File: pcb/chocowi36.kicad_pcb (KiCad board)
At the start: 2 copper layers, 113.1 x 88.3 mm, 29 parts, among them SW10 SW_Push, SW11 SW_Push, SW12 SW_Push, SW14 SW_Push, SW15 SW_Push, SW16 SW_Push, SW17 SW_Push, SW18 SW_Push, SW19 SW_Push, SW2 SW_Push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

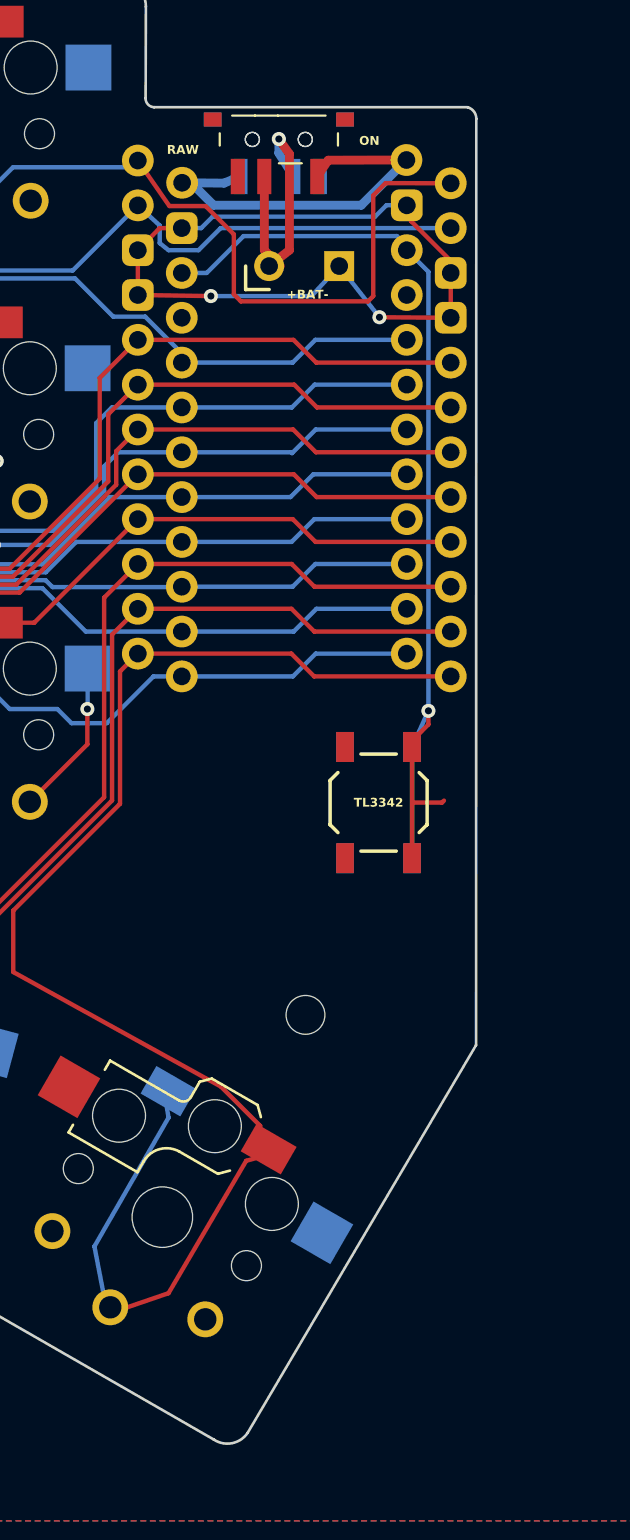
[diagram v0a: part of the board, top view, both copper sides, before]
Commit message: add tp4056 charging module, update edge.cut
change power button position
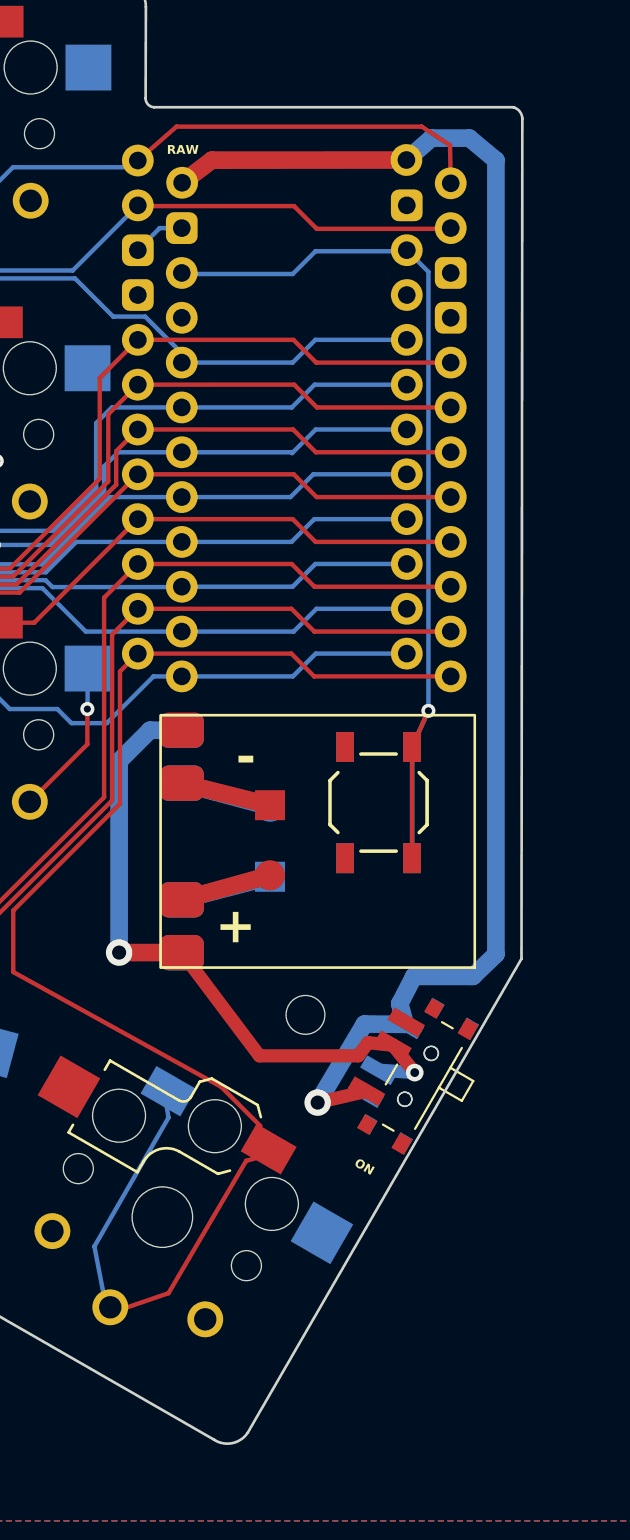
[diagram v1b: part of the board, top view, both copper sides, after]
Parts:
- added BT2: B1, itsdmd:Battery_Pads-dual-side, B.Cu at (176.6, 101.4)
- added T1: ~, itsdmd:Module_TP4056_Mini-SMD_Interface, F.Cu at (179.2, 101.5)
- added T2: ~, itsdmd:Module_TP4056_Mini-SMD_Interface, B.Cu at (179.2, 101.5)
- BT1: value Battery_Cell -> B1
- moved SW_POWER1 53.8 mm to (184.8, 115.0), turned to 60 degrees
- moved SW_POWER2 53.6 mm to (185.0, 114.7), turned to -120 degrees
- moved BT1 32.7 mm to (176.6, 101.5), turned to 90 degrees
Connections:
- BT1 pad 2: gnd -> Net-(BT1--)
- SW_POWER1 pad COM: Net-(BT1-+) -> Net-(T1-Load+)
- SW_POWER2 pad COM: Net-(BT1-+) -> Net-(T1-Load+)
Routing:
- net +BATT: track 23.2 -> 82.6 mm, vias 0 -> 1
- net gnd: track 55.8 -> 12.9 mm, vias 3 -> 1
- net Net-(T1-Load+): track 0.00 -> 38.2 mm, vias 0 -> 2
- net Net-(BT1-+): track 15.7 -> 5.19 mm, vias 1 -> 0
- net Switch6: track 69.5 -> 61.0 mm
- net Net-(BT2-+): track 0.00 -> 5.18 mm
- net Net-(BT2--): track 0.00 -> 5.17 mm
- net Net-(BT1--): track 0.00 -> 5.15 mm
- net reset: track 59.8 -> 57.0 mm
- net Switch5: track 79.4 -> 77.9 mm
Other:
- board size 113.1 x 88.3 mm -> 115.7 x 88.3 mm
- board text removed: "+BAT-"
- board text removed: "-BAT+"

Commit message: minor improvements
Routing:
- net gnd: track 12.9 -> 9.84 mm
- net reset: track 57.0 -> 57.7 mm

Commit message: slight changes
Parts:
- moved BT1 11.6 mm to (166.4, 107.1)
- moved BT2 11.6 mm to (166.4, 107.0)
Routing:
- net Net-(BT1--): track 5.15 -> 8.58 mm
- net Net-(BT2-+): track 5.18 -> 8.58 mm
- net Net-(T1-Load+): track 38.2 -> 39.9 mm
- net Net-(BT2--): track 5.17 -> 6.66 mm
- net Net-(BT1-+): track 5.19 -> 6.66 mm
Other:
- board text added: "+"
